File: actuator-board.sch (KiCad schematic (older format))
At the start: 22 parts, among them J1 CONN_IO, J2 CONN_PWM, U1 STM32F302K8U6, U2 MCP1703, U3 MAX3051, X1 16MHz 10ppm

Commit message: Start actuator-board
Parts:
- C1, C10, C2, C3, C4, C5, C6, C7, C8, C9: symbol can-io-board-rescue:C-device -> actuator-board-rescue:C-device
- CONN1: symbol can-io-board-rescue:SWD_DEBUG -> actuator-board-rescue:SWD_DEBUG
- D1: symbol can-io-board-rescue:LED -> actuator-board-rescue:LED
- R1: symbol can-io-board-rescue:R-device -> actuator-board-rescue:R-device
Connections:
- wire segments 120 -> 121
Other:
- note added: "2x pump half bridge\n2x solenoid half bridge\n2x vacuum sensor SPI + 2x CS\n1-2 Servo PWM\n1-2 analog input\n1-2 digital input"
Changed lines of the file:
@@
 EESchema Schematic File Version 4
-LIBS:can-io-board-cache
+LIBS:actuator-board-cache
 EELAYER 26 0
 EELAYER END
@@
 3.3V
 $Comp
-L can-io-board-rescue:C-device C9
+L actuator-board-rescue:C-device C9
 U 1 1 56D60C22
 P 8300 3100
@@
 $EndComp
 $Comp
-L can-io-board-rescue:C-device C10
+L actuator-board-rescue:C-device C10
 U 1 1 56D60C4F
 P 9500 3100
@@
 $EndComp
 $Comp
-L can-io-board-rescue:C-device C8
+L actuator-board-rescue:C-device C8
 U 1 1 56D610D6
 P 7450 4900
@@
 5V_CAN
 $Comp
-L can-io-board-rescue:C-device C5
+L actuator-board-rescue:C-device C5
 U 1 1 56D62888
 P 3600 3800
@@
 $EndComp
 $Comp
-L can-io-board-rescue:C-device C1
+L actuator-board-rescue:C-device C1
 U 1 1 56D628FF
 P 3100 3800
@@
 $EndComp
 $Comp
-L can-io-board-rescue:C-device C3
+L actuator-board-rescue:C-device C3
 U 1 1 56D6293B
 P 3500 4350
@@
 $EndComp
 $Comp
-L can-io-board-rescue:C-device C2
+L actuator-board-rescue:C-device C2
 U 1 1 56D62D2B
 P 3350 3800
@@
 $EndComp
 $Comp
-L can-io-board-rescue:C-device C4
+L actuator-board-rescue:C-device C4
 U 1 1 56D635F0
 P 3550 3250
@@
 $EndComp
 $Comp
-L can-io-board-rescue:C-device C6
+L actuator-board-rescue:C-device C6
 U 1 1 56D63ACC
 P 5600 6000
@@
 $EndComp
 $Comp
-L can-io-board-rescue:C-device C7
+L actuator-board-rescue:C-device C7
 U 1 1 56D63B8B
 P 6300 6000
@@
 $EndComp
 $Comp
-L can-io-board-rescue:LED D1
+L actuator-board-rescue:LED D1
 U 1 1 56D63FB2
 P 1450 4950
@@
 $EndComp
 $Comp
-L can-io-board-rescue:R-device R1
+L actuator-board-rescue:R-device R1
 U 1 1 56D64054
 P 1450 4550
@@
 IO_PB7_I2C1SDA_UART1RX
 $Comp
-L can-io-board-rescue:SWD_DEBUG CONN1
+L actuator-board-rescue:SWD_DEBUG CONN1
 U 1 1 56D60ADA
 P 1400 1800
@@
 Wire Wire Line
 	7150 2900 7750 2900
+Wire Wire Line
+	7150 2900 7750 2900
+Text Notes 5050 1700 0    60   ~ 0
+2x pump half bridge\n2x solenoid half bridge\n2x vacuum sensor SPI + 2x CS\n1-2 Servo PWM\n1-2 analog input\n1-2 digital input
 $EndSCHEMATC

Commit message: pin assignment WIP
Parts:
- removed J1: CONN_IO, Connector_Molex:Molex_PicoBlade_53261-0871_1x08-1MP_P1.25mm_Horizontal, symbol Connector_Generic:Conn_02x04_Odd_Even
- removed J2: CONN_PWM, Connector_Molex:Molex_PicoBlade_53261-0871_1x08-1MP_P1.25mm_Horizontal, symbol Connector_Generic:Conn_02x04_Odd_Even
- C1, C10, C2, C3, C4, C5, C6, C7, C8, C9: symbol actuator-board-rescue:C-device -> Device:C
- CONN1: symbol actuator-board-rescue:SWD_DEBUG -> _connectors:SWD_DEBUG
- D1: symbol actuator-board-rescue:LED -> Device:LED
- R1: symbol actuator-board-rescue:R-device -> Device:R
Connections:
- net labels added: ANALOG1, ANALOG2, PUMP1_PA6_TIM16_CH1, PUMP2_PA7_TIM17_CH1, SERVO1_PA9_TIM1_CH2, SERVO2_PA10_TIM1_CH3, SPI3_MISO, SPI3_MOSI, SPI3_SCK, VACUUM_SENS1_CS, VACUUM_SENS_RESET, VALVE1, VALVE2
- net labels removed: IO0_PA0, IO1_PA1, IO2_PA2, IO3_PA3, IO_PB7_I2C1SDA_UART1RX, PWM0_PA6_TIM16_CH1, PWM1_PA7_TIM17_CH1, PWM2_PA9_TIM1_CH2, PWM3_PA10_TIM1_CH3
- wire segments 121 -> 106
- no-connect marks 7 -> 1
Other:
- note added: "(JTDO/SWO)"
- note added: "(JTRST)"
- note removed: "JTDO/SWO"
- note removed: "JTRST"
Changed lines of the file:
@@
 EESchema Schematic File Version 4
 LIBS:actuator-board-cache
-EELAYER 26 0
+EELAYER 30 0
 EELAYER END
 $Descr A4 11693 8268
@@
 3.3V
 $Comp
-L actuator-board-rescue:C-device C9
+L Device:C C9
 U 1 1 56D60C22
 P 8300 3100
@@
 $EndComp
 $Comp
-L actuator-board-rescue:C-device C10
+L Device:C C10
 U 1 1 56D60C4F
 P 9500 3100
@@
 $EndComp
 $Comp
-L actuator-board-rescue:C-device C8
+L Device:C C8
 U 1 1 56D610D6
 P 7450 4900
@@
 5V_CAN
 $Comp
-L actuator-board-rescue:C-device C5
+L Device:C C5
 U 1 1 56D62888
 P 3600 3800
@@
 $EndComp
 $Comp
-L actuator-board-rescue:C-device C1
+L Device:C C1
 U 1 1 56D628FF
 P 3100 3800
@@
 $EndComp
 $Comp
-L actuator-board-rescue:C-device C3
+L Device:C C3
 U 1 1 56D6293B
 P 3500 4350
@@
 $EndComp
 $Comp
-L actuator-board-rescue:C-device C2
+L Device:C C2
 U 1 1 56D62D2B
 P 3350 3800
@@
 L power:GND #PWR010
 U 1 1 56D634B2
-P 3800 3250
-F 0 "#PWR010" H 3800 3000 50  0001 C CNN
-F 1 "GND" H 3800 3100 50  0000 C CNN
-F 2 "" H 3800 3250 50  0000 C CNN
-F 3 "" H 3800 3250 50  0000 C CNN
-	1    3800 3250
-	1    0    0    -1
-$EndComp
-$Comp
-L actuator-board-rescue:C-device C4
+P 3850 3250
+F 0 "#PWR010" H 3850 3000 50  0001 C CNN
+F 1 "GND" H 3850 3100 50  0000 C CNN
+F 2 "" H 3850 3250 50  0000 C CNN
+F 3 "" H 3850 3250 50  0000 C CNN
+	1    3850 3250
+	1    0    0    -1
+$EndComp
+$Comp
+L Device:C C4
 U 1 1 56D635F0
 P 3550 3250
@@
 L power:GND #PWR011
 U 1 1 56D636C6
-P 3550 3450
-F 0 "#PWR011" H 3550 3200 50  0001 C CNN
-F 1 "GND" H 3550 3300 50  0000 C CNN
-F 2 "" H 3550 3450 50  0000 C CNN
-F 3 "" H 3550 3450 50  0000 C CNN
-	1    3550 3450
-	1    0    0    -1
-$EndComp
-$Comp
-L actuator-board-rescue:C-device C6
+P 3550 3400
+F 0 "#PWR011" H 3550 3150 50  0001 C CNN
+F 1 "GND" H 3550 3250 50  0000 C CNN
+F 2 "" H 3550 3400 50  0000 C CNN
+F 3 "" H 3550 3400 50  0000 C CNN
+	1    3550 3400
+	1    0    0    -1
+$EndComp
+$Comp
+L Device:C C6
 U 1 1 56D63ACC
 P 5600 6000
@@
 $EndComp
 $Comp
-L actuator-board-rescue:C-device C7
+L Device:C C7
 U 1 1 56D63B8B
 P 6300 6000
@@
 $EndComp
 $Comp
-L actuator-board-rescue:LED D1
+L Device:LED D1
 U 1 1 56D63FB2
 P 1450 4950
@@
 $EndComp
 $Comp
-L actuator-board-rescue:R-device R1
+L Device:R R1
 U 1 1 56D64054
 P 1450 4550
@@
 Text Label 1450 4350 0    60   ~ 0
 LED
-Text Label 5450 3500 0    60   ~ 0
+Text Label 5450 4600 0    60   ~ 0
 LED
 $Comp
@@
 Text Label 5450 5300 0    60   ~ 0
 IO_PB6_I2C1SCL_UART1TX
-Text Label 5450 5400 0    60   ~ 0
-IO_PB7_I2C1SDA_UART1RX
-Text Notes 5550 5100 0    60   ~ 0
-JTRST
+Text Notes 6050 5100 0    60   ~ 0
+(JTRST)
 Text Label 1800 2000 0    60   ~ 0
 IO_PB6_I2C1SCL_UART1TX
-Text Label 1800 2100 0    60   ~ 0
-IO_PB7_I2C1SDA_UART1RX
-$Comp
-L actuator-board-rescue:SWD_DEBUG CONN1
+$Comp
+L _connectors:SWD_DEBUG CONN1
 U 1 1 56D60ADA
 P 1400 1800
@@
 	-1   0    0    -1
 $EndComp
-NoConn ~ 5350 3600
-NoConn ~ 5350 3900
 Wire Wire Line
 	5350 3800 5450 3800
 Wire Wire Line
-	5350 3700 5450 3700
-Wire Wire Line
 	5450 4100 5350 4100
 Wire Wire Line
 	5450 4000 5350 4000
 Wire Wire Line
-	1800 2100 1750 2100
-Wire Wire Line
 	1750 2000 1800 2000
 Wire Wire Line
-	5450 5400 5350 5400
-Wire Wire Line
 	5450 5300 5350 5300
 Wire Wire Line
@@
 Wire Wire Line
 	5350 4400 5450 4400
-Wire Wire Line
-	3400 3100 3550 3100
 Wire Wire Line
 	8100 5050 8200 5050
@@
 Connection ~ 3100 4000
 Connection ~ 3100 3600
-Connection ~ 3500 4200
-Connection ~ 3500 4500
 Wire Wire Line
 	1450 4350 1450 4400
 Wire Wire Line
-	1450 4700 1450 4750
-Wire Wire Line
-	1450 5200 1450 5150
-Connection ~ 5600 5850
-Connection ~ 6300 5850
+	1450 4700 1450 4800
+Wire Wire Line
+	1450 5200 1450 5100
 Wire Wire Line
 	6300 5600 6300 5850
@@
 Wire Wire Line
 	5600 5850 5650 5850
-Connection ~ 3550 3100
-Wire Wire Line
-	3550 3450 3550 3400
-Wire Wire Line
-	3800 3200 3850 3200
-Wire Wire Line
-	3800 3250 3800 3200
+Wire Wire Line
+	3850 3250 3850 3200
 Wire Wire Line
 	1750 1900 1800 1900
@@
 	2100 1500 2100 1450
 Wire Wire Line
-	3750 4500 3500 4500
-Wire Wire Line
 	3750 4300 3750 4500
 Wire Wire Line
 	3850 4300 3750 4300
-Wire Wire Line
-	3250 4200 3500 4200
 Connection ~ 3350 4000
 Wire Wire Line
@@
 	1    0    0    -1
 $EndComp
-NoConn ~ 5350 4600
-Wire Wire Line
-	5450 3500 5350 3500
 Wire Wire Line
 	3100 4000 3350 4000
@@
 	3100 3600 3350 3600
 Wire Wire Line
-	3500 4200 3850 4200
-Wire Wire Line
-	3500 4500 3250 4500
-Wire Wire Line
 	5900 6150 5950 6150
 Wire Wire Line
@@
 Wire Wire Line
 	5950 6150 6000 6150
-Wire Wire Line
-	3550 3100 3850 3100
 Wire Wire Line
 	3350 4000 3600 4000
@@
 	1    0    0    -1
 $EndComp
-NoConn ~ 5350 4850
 $Comp
 L power:GND #PWR0101
@@
 	1    0    0    -1
 $EndComp
-Text Label 4350 1650 0    60   ~ 0
-PWM2_PA9_TIM1_CH2
-Text Label 4350 1750 0    60   ~ 0
-PWM3_PA10_TIM1_CH3
-Text Label 4350 1550 0    60   ~ 0
-PWM1_PA7_TIM17_CH1
-Text Label 4350 1450 0    60   ~ 0
-PWM0_PA6_TIM16_CH1
-Text Notes 5550 5000 0    60   ~ 0
-JTDO/SWO
-NoConn ~ 5350 5200
-NoConn ~ 5350 5100
-NoConn ~ 5350 5000
-Text Label 6450 1550 0    60   ~ 0
-IO1_PA1
-Text Label 6450 1450 0    60   ~ 0
-IO0_PA0
-Text Label 6450 1650 0    60   ~ 0
-IO2_PA2
-Text Label 6450 1750 0    60   ~ 0
-IO3_PA3
+Text Notes 6050 5000 0    60   ~ 0
+(JTDO/SWO)
 Connection ~ 3850 3600
 Connection ~ 3850 4000
@@
 	5450 3400 5350 3400
 Text Label 5450 4000 0    60   ~ 0
-PWM2_PA9_TIM1_CH2
+SERVO1_PA9_TIM1_CH2
 Text Label 5450 4100 0    60   ~ 0
-PWM3_PA10_TIM1_CH3
+SERVO2_PA10_TIM1_CH3
 Text Label 5450 3800 0    60   ~ 0
-PWM1_PA7_TIM17_CH1
-Text Label 5450 3700 0    60   ~ 0
-PWM0_PA6_TIM16_CH1
-$Comp
-L Connector_Generic:Conn_02x04_Odd_Even J1
-U 1 1 5BCE6632
-P 5600 1550
-F 0 "J1" H 5650 1867 50  0000 C CNN
-F 1 "CONN_IO" H 5650 1776 50  0000 C CNN
-F 2 "Connector_Molex:Molex_PicoBlade_53261-0871_1x08-1MP_P1.25mm_Horizontal" H 5600 1550 50  0001 C CNN
-F 3 "~" H 5600 1550 50  0001 C CNN
-	1    5600 1550
-	1    0    0    -1
-$EndComp
-Wire Wire Line
-	5400 1450 4350 1450
-Wire Wire Line
-	4350 1550 5400 1550
-Wire Wire Line
-	5400 1650 4350 1650
-Wire Wire Line
-	5400 1750 4350 1750
-$Comp
-L power:GND #PWR0102
-U 1 1 5BCF9CD0
-P 6050 1750
-F 0 "#PWR0102" H 6050 1500 50  0001 C CNN
-F 1 "GND" H 6050 1600 50  0000 C CNN
-F 2 "" H 6050 1750 50  0000 C CNN
-F 3 "" H 6050 1750 50  0000 C CNN
-	1    6050 1750
-	-1   0    0    -1
-$EndComp
-Wire Wire Line
-	5900 1450 5900 1550
-Wire Wire Line
-	5900 1750 6050 1750
-Connection ~ 5900 1750
-Connection ~ 5900 1550
-Wire Wire Line
-	5900 1550 5900 1650
-Connection ~ 5900 1650
-Wire Wire Line
-	5900 1650 5900 1750
-$Comp
-L Connector_Generic:Conn_02x04_Odd_Even J2
-U 1 1 5BCFEFB5
-P 7150 1550
-F 0 "J2" H 7200 1867 50  0000 C CNN
-F 1 "CONN_PWM" H 7200 1776 50  0000 C CNN
-F 2 "Connector_Molex:Molex_PicoBlade_53261-0871_1x08-1MP_P1.25mm_Horizontal" H 7150 1550 50  0001 C CNN
-F 3 "~" H 7150 1550 50  0001 C CNN
-	1    7150 1550
-	1    0    0    -1
-$EndComp
-Wire Wire Line
-	7450 1450 7450 1550
-Wire Wire Line
-	7450 1750 7600 1750
-Connection ~ 7450 1750
-Connection ~ 7450 1550
-Wire Wire Line
-	7450 1550 7450 1650
-Connection ~ 7450 1650
-Wire Wire Line
-	7450 1650 7450 1750
-$Comp
-L power:GND #PWR0103
-U 1 1 5BD1EF19
-P 7600 1750
-F 0 "#PWR0103" H 7600 1500 50  0001 C CNN
-F 1 "GND" H 7600 1600 50  0000 C CNN
-F 2 "" H 7600 1750 50  0000 C CNN
-F 3 "" H 7600 1750 50  0000 C CNN
-	1    7600 1750
-	-1   0    0    -1
-$EndComp
-Wire Wire Line
-	6950 1450 6450 1450
-Wire Wire Line
-	6450 1550 6950 1550
-Wire Wire Line
-	6450 1650 6950 1650
-Wire Wire Line
-	6450 1750 6950 1750
+PUMP2_PA7_TIM17_CH1
 Text Label 5450 3200 0    60   ~ 0
-IO1_PA1
+ANALOG2
 Text Label 5450 3100 0    60   ~ 0
-IO0_PA0
-Text Label 5450 3300 0    60   ~ 0
-IO2_PA2
-Text Label 5450 3400 0    60   ~ 0
-IO3_PA3
+ANALOG1
 Wire Wire Line
 	8100 5050 8100 5150
@@
 Wire Wire Line
 	7150 2900 7750 2900
-Wire Wire Line
-	7150 2900 7750 2900
-Text Notes 5050 1700 0    60   ~ 0
+Text Notes 2350 6300 0    60   ~ 0
 2x pump half bridge\n2x solenoid half bridge\n2x vacuum sensor SPI + 2x CS\n1-2 Servo PWM\n1-2 analog input\n1-2 digital input
+Wire Wire Line
+	3400 3100 3550 3100
+Wire Wire Line
+	3250 4500 3750 4500
+Wire Wire Line
+	3250 4200 3850 4200
+NoConn ~ 1750 2100
+Wire Wire Line
+	5350 3700 5450 3700
+Text Label 5450 3700 0    60   ~ 0
+PUMP1_PA6_TIM16_CH1
+Wire Wire Line
+	5350 3600 5450 3600
+Text Label 5450 3500 0    60   ~ 0
+VALVE1
+Text Label 5450 3600 0    60   ~ 0
+VALVE2
+Wire Wire Line
+	5450 3900 5350 3900
+Text Label 5450 5200 0    60   ~ 0
+SPI3_MOSI
+Text Label 5450 5100 0    60   ~ 0
+SPI3_MISO
+Text Label 5450 5000 0    60   ~ 0
+SPI3_SCK
+Wire Wire Line
+	5350 5000 5450 5000
+Wire Wire Line
+	5350 5100 5450 5100
+Wire Wire Line
+	5350 5200 5450 5200
+Text Label 5450 4850 0    60   ~ 0
+VACUUM_SENS1_CS
+Wire Wire Line
+	5350 4850 5450 4850
+Text Label 5450 5400 0    60   ~ 0
+VACUUM_SENS1_CS
+Wire Wire Line
+	5450 5400 5350 5400
+Wire Wire Line
+	5450 4600 5350 4600
+Wire Wire Line
+	5350 3500 5450 3500
+Text Label 7300 4150 0    60   ~ 0
+VACUUM_SENS_RESET
+Connection ~ 3550 3100
+Wire Wire Line
+	3550 3100 3850 3100
 $EndSCHEMATC

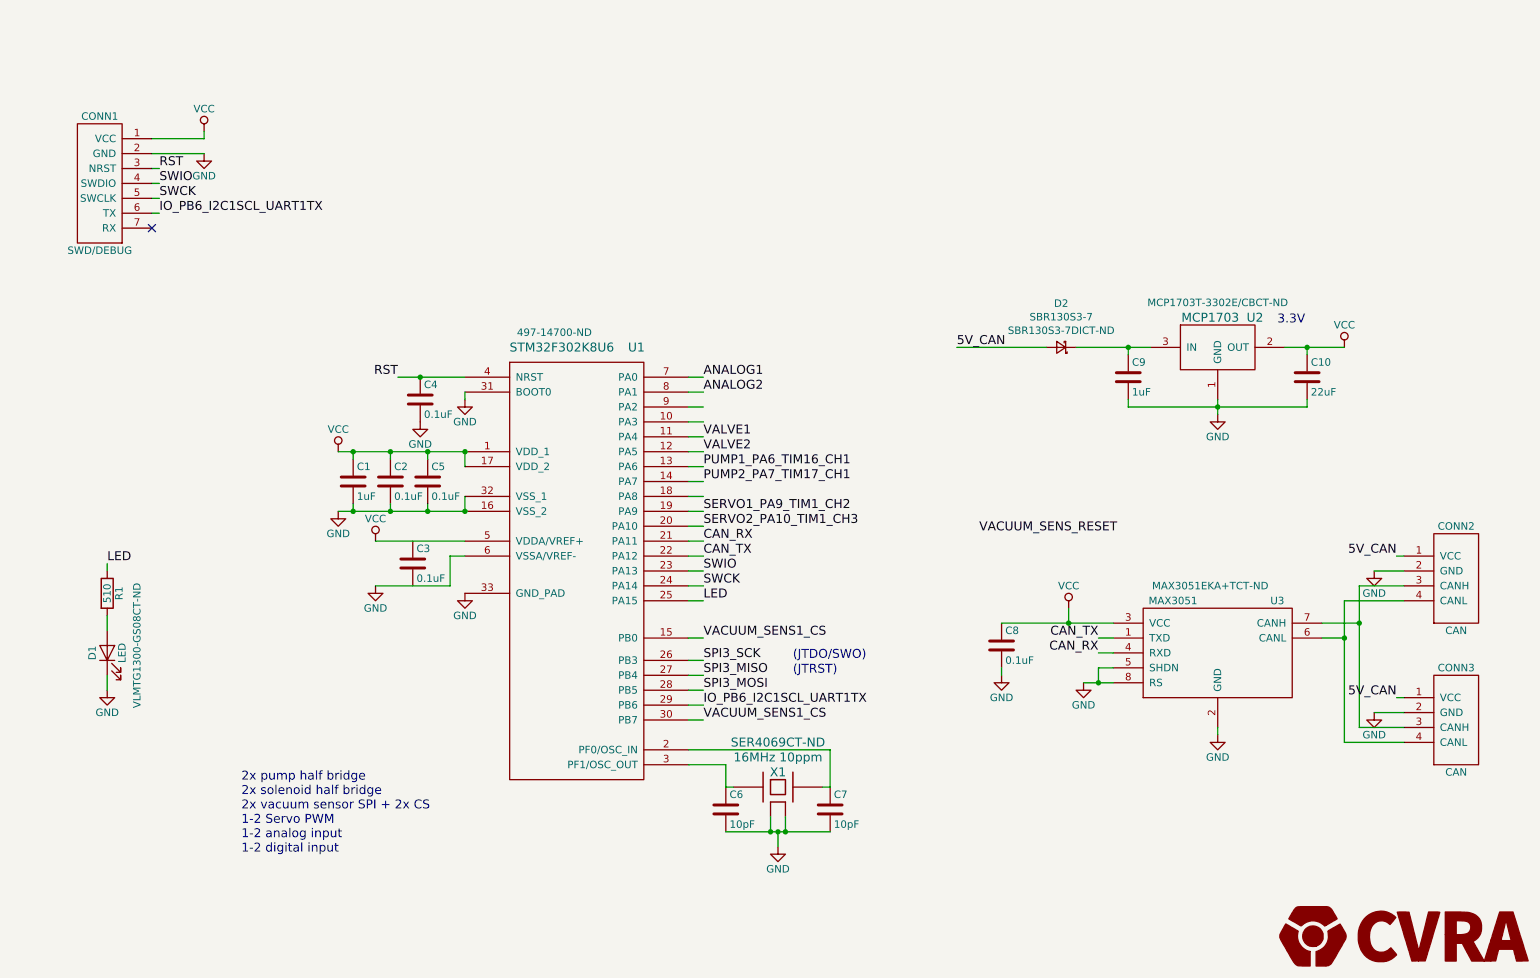
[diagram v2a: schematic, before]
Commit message: Finish the design of th actuator board schematic
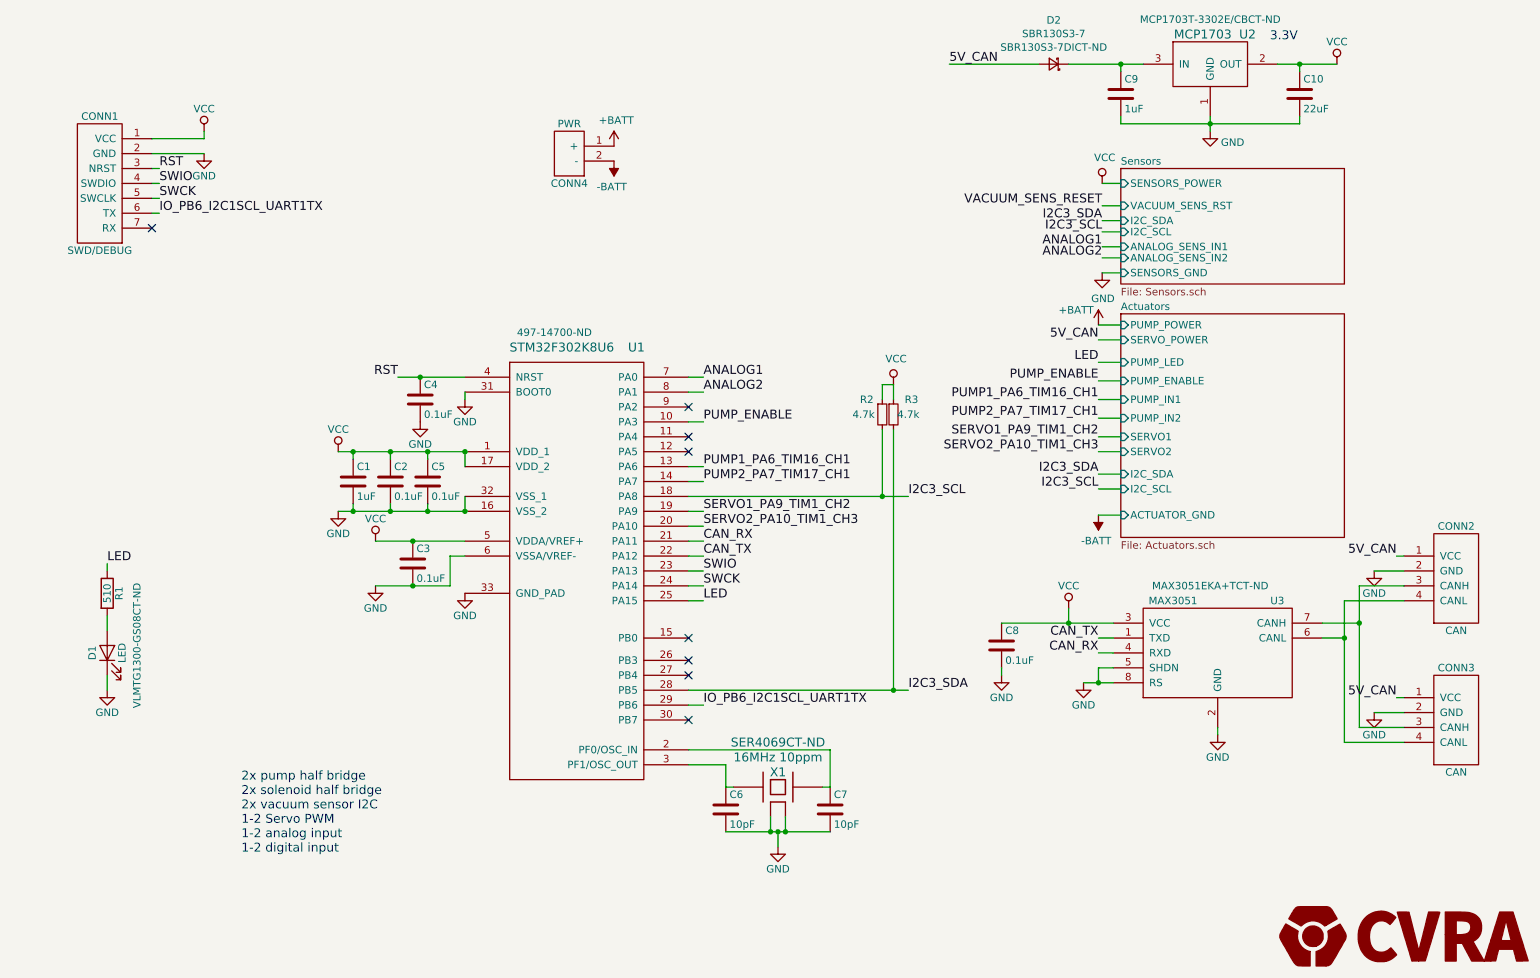
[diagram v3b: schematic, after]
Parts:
- added CONN4: PWR, MODULE, symbol _connectors:PWR
- added R2, R3: 4.7k, symbol Device:R_Small
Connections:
- net GND: now also C3.2, CONN4.MECH (GND)
- net VCC: now also C3.1, R2.1, R3.1
- net PUMP_ENABLE: now reaches U1.10 (PA3)
- net I2C3_SCL: now reaches U1.18 (PA8)
- net I2C3_SCL: now also R2.2
- net SPI3_MISO: no longer names the net of U1.27 (PB4)
- net SPI3_MOSI renamed I2C3_SDA
- net I2C3_SDA: now also R3.2
- net SPI3_SCK: no longer names the net of U1.26 (PB3)
- net VACUUM_SENS1_CS: no longer names the net of U1.15 (PB0)
- net VACUUM_SENS1_CS: no longer U1.30 (PB7)
- net VALVE1: no longer names the net of U1.11 (PA4)
- net VALVE2: no longer names the net of U1.12 (PA5)
- new net +BATT: CONN4.1 (+)
- new net -BATT: CONN4.2 (-)
- no-connect marks 1 -> 8
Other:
- note added: "2x pump half bridge\n2x solenoid half bridge\n2x vacuum sensor I2C\n1-2 Servo PWM\n1-2 analog input\n1-2 digital input"
- note removed: "(JTDO/SWO)"
- note removed: "(JTRST)"
- note removed: "2x pump half bridge\n2x solenoid half bridge\n2x vacuum sensor SPI + 2x CS\n1-2 Servo PWM\n1-2 analog input\n1-2 digital input"
- moved on the sheet: C10, C9, D2, U2
